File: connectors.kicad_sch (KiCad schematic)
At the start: 0 parts

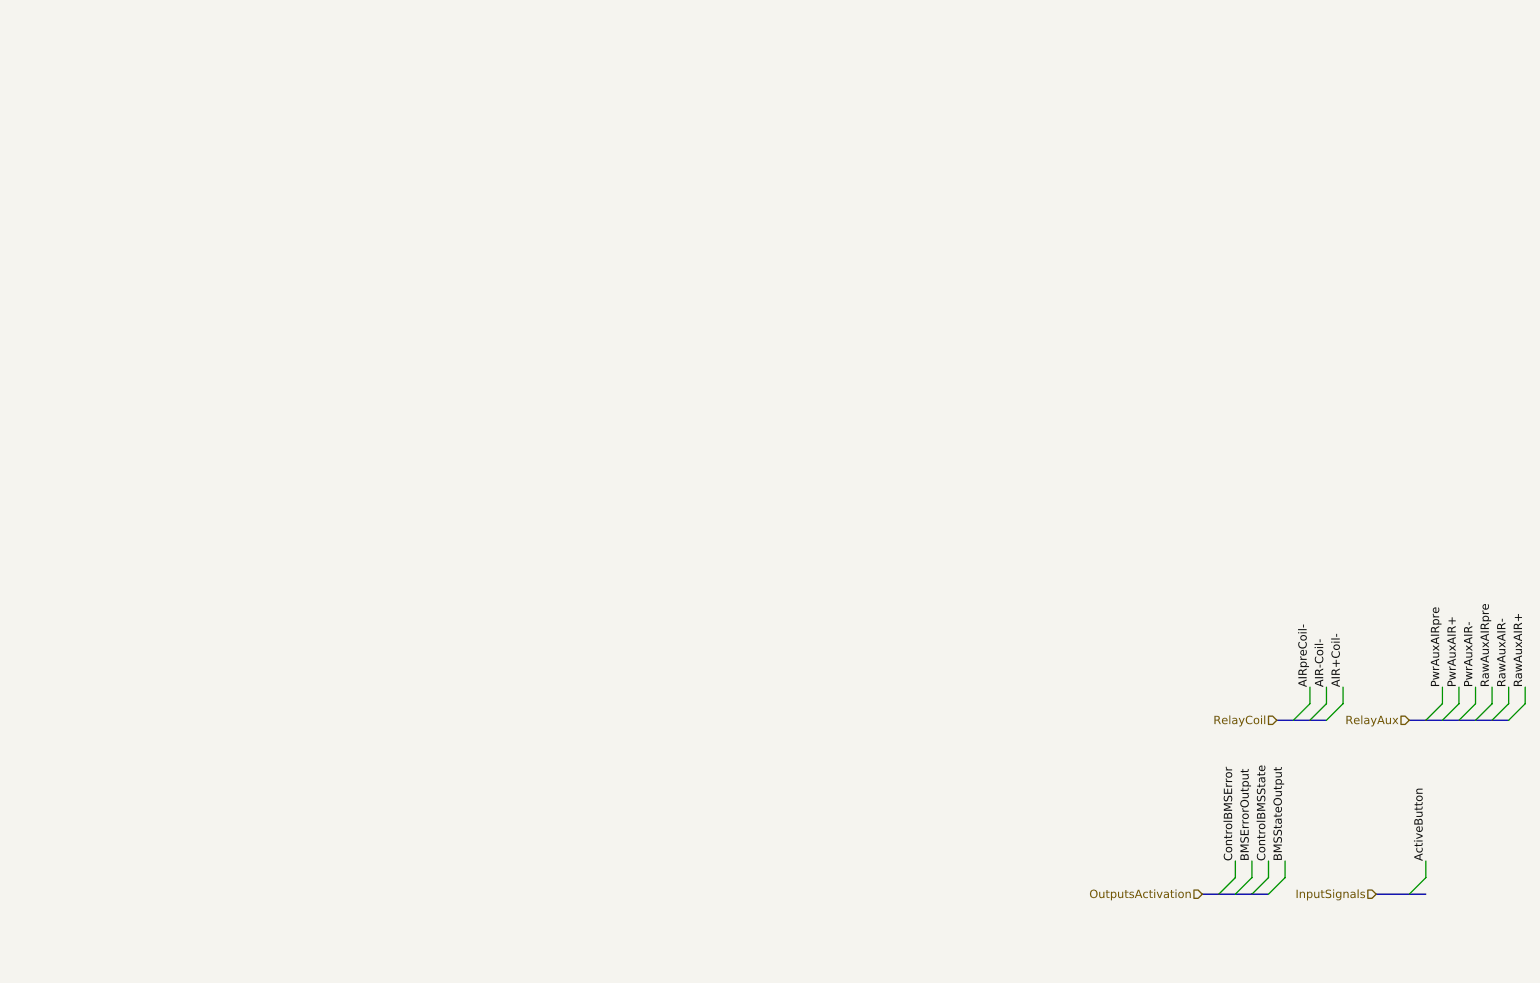
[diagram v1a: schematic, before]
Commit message: - S'han afegit uns connectors preliminar \n-S'han eliminat els diodes de protecció dels airs
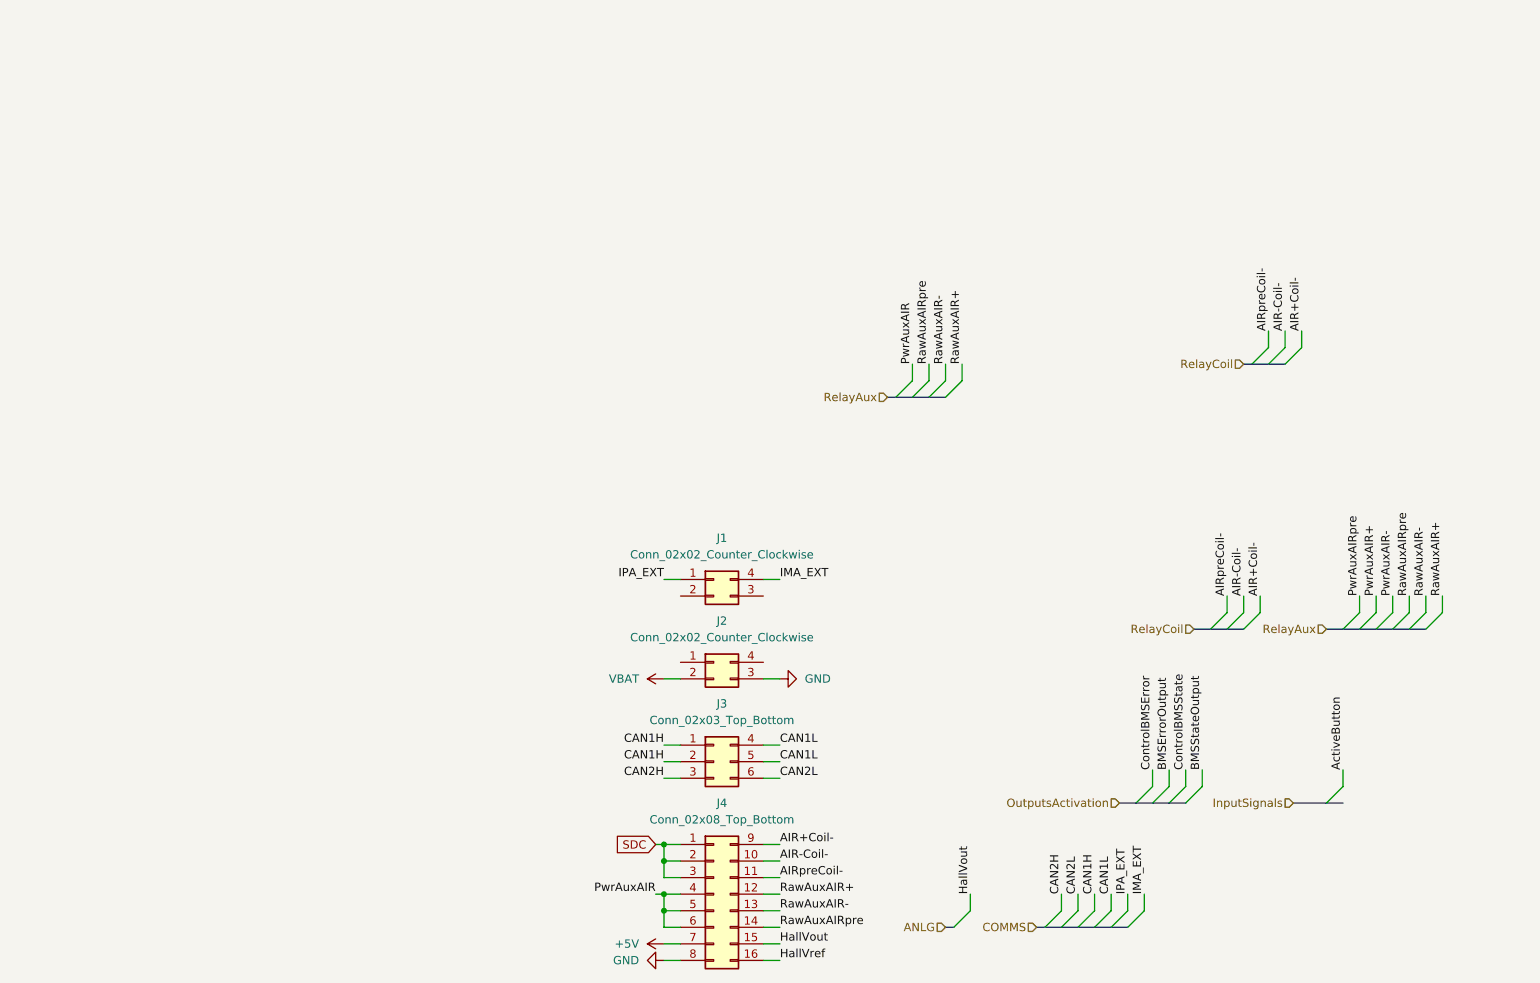
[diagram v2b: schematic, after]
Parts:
- added J1, J2: Conn_02x02_Counter_Clockwise, Connector_Molex:Molex_Nano-Fit_105314-xx04_2x02_P2.50mm_Horizontal, symbol Connector_Generic:Conn_02x02_Counter_Clockwise
- added J3: Conn_02x03_Top_Bottom, Connector_Molex:Molex_Nano-Fit_105314-xx06_2x03_P2.50mm_Horizontal, symbol Connector_Generic:Conn_02x03_Top_Bottom
- added J4: Conn_02x08_Top_Bottom, Connector_Molex:Molex_Nano-Fit_105314-xx16_2x08_P2.50mm_Horizontal, symbol Connector_Generic:Conn_02x08_Top_Bottom
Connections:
- net AIR+Coil-: now also J4.9 (Pin_9)
- net AIR-Coil-: now also J4.10 (Pin_10)
- net AIRpreCoil-: now also J4.11 (Pin_11)
- net RawAuxAIR+: now also J4.12 (Pin_12)
- net RawAuxAIR-: now also J4.13 (Pin_13)
- net RawAuxAIRpre: now also J4.14 (Pin_14)
- new net +5V: J4.7 (Pin_7)
- new net CAN1H: J3.1 (Pin_1), J3.2 (Pin_2)
- new net CAN1L: J3.4 (Pin_4), J3.5 (Pin_5)
- new net CAN2H: J3.3 (Pin_3)
- new net CAN2L: J3.6 (Pin_6)
- new net GND: J2.3 (Pin_3), J4.8 (Pin_8)
- new net HallVout: J4.15 (Pin_15)
- new net HallVref: J4.16 (Pin_16)
- new net IMA_EXT: J1.4 (Pin_4)
- new net IPA_EXT: J1.1 (Pin_1)
- new net PwrAuxAIR: J4.4 (Pin_4), J4.5 (Pin_5), J4.6 (Pin_6)
- new net SDC: J4.1 (Pin_1), J4.2 (Pin_2), J4.3 (Pin_3)
- new net VBAT: J2.2 (Pin_2)

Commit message: Modificació de les etiquetes a globals Filtre afegit al transformador de isoSPI Leds indicadors per estat i error Senyal d'error de BMS per el sdcreset
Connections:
- net IMA_EXT: no longer J1.4 (Pin_4)
- net IPA_EXT: no longer J1.1 (Pin_1)
- new net isoIMA: J1.4 (Pin_4)
- new net isoIPA: J1.1 (Pin_1)
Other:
- moved on the sheet: J1, J2, J3, J4
